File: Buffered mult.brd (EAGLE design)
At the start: 100.4 x 17.6 mm, 29 parts, among them IC1 OPA4171, IC3 OPA4171, J1 EURO_POWER_HEADERFAT_PADS

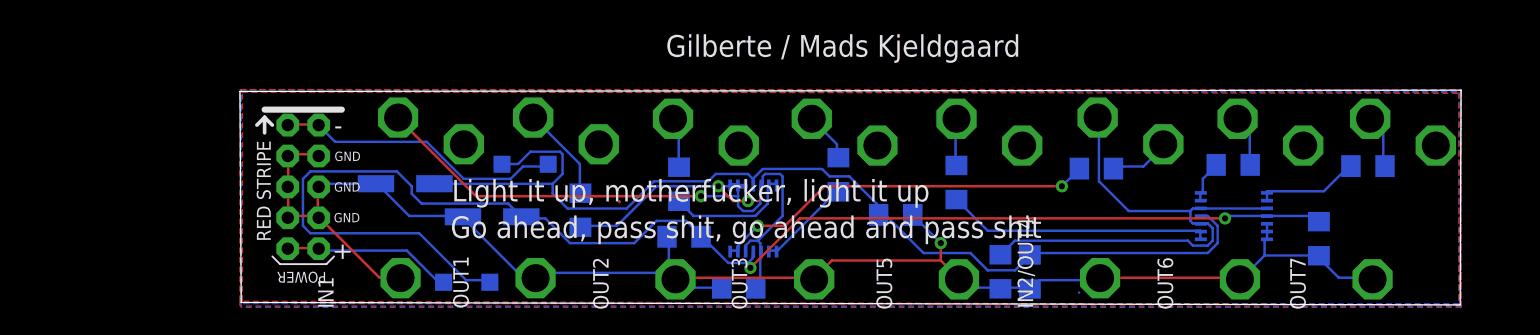
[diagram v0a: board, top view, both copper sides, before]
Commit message: new revision: Changed IC2 to opa2171, fixed switch jack
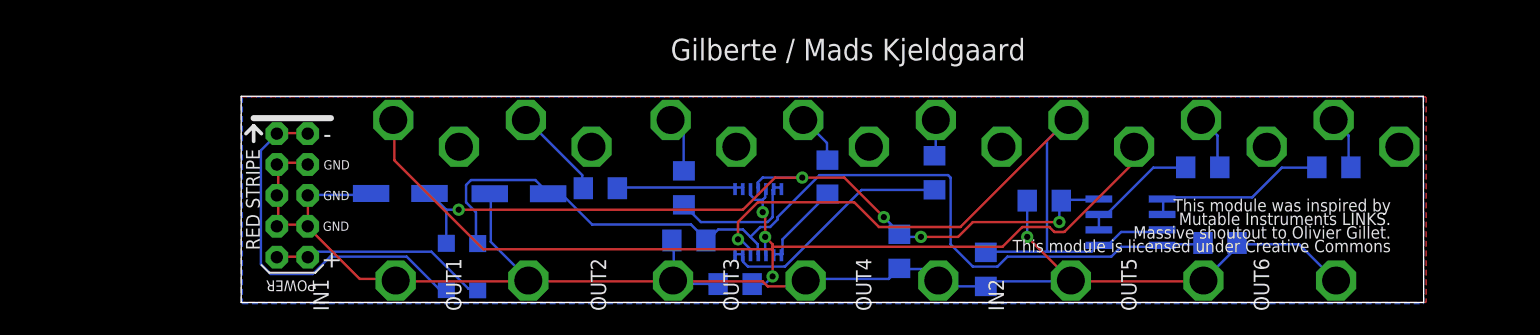
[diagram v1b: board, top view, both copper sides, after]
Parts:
- removed IC3: OPA4171, linear:TSSOP14
- removed IN2/OUT4, OUT7: PJ302M, pj302m:PJ302M
- removed R9: 51, SparkFun-Passives:1206
- added IC4: OPA2171, linear:SO08
- added IN2, OUT4: PJ302M, pj302m:PJ302M
- moved OUT5 20.1 mm to (79.1, -0.70)
- moved D1 10.6 mm to (16.9, 2.96), turned to 270 degrees
- moved C3 8.14 mm to (80.5, 4.89), turned to 0 degrees
- moved OUT6 7.90 mm to (90.0, -0.70)
- moved C2 5.98 mm to (66.0, 8.37), turned to 0 degrees
- moved C5 3.01 mm to (54.1, 4.20), turned to 270 degrees
- moved C13 2.91 mm to (22.8, 8.94)
- moved R6 2.80 mm to (89.8, 11.1)
- moved R5 2.51 mm to (79.0, 11.1)
- moved R3 2.44 mm to (29.5, 9.39), turned to 0 degrees
- moved R4 1.97 mm to (57.0, 10.7)
- moved D2 1.56 mm to (19.4, 2.94), turned to 90 degrees
- moved R8 1.22 mm to (61.2, 2.72)
- moved J1 1.14 mm to (4.20, 8.80)
- moved R2 0.92 mm to (48.2, 10.3)
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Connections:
- removed net N$16: IC1.13, IC1.14, R9.1
- removed net N$18: IN2/OUT4.SW, R9.2
- net GND: now also IN2.GND, OUT4.GND; no longer IC3.12, IC3.13, IC3.14, IN2/OUT4.GND, OUT7.GND
- net N$1: now also OUT6.TIP; no longer OUT7.TIP
- net N$12: now also IC4.1, IC4.2; no longer IC3.8, IC3.9
- net N$13: now also IC4.6, IC4.7; no longer IC3.6, IC3.7
- net N$17: now also IC1.13, IC1.14; no longer IC3.1, IC3.2
- net N$19: now also IC1.12, IC4.3, IC4.5, IN2.TIP; no longer IC3.10, IC3.3, IC3.5, IN2/OUT4.TIP
- net N$3: now also OUT5.TIP; no longer OUT6.TIP
- net N$4: now also OUT4.TIP; no longer OUT5.TIP
- net N$5: now also IN2.SW; no longer IC1.12
- net VCC: now also IC4.8; no longer IC3.4
- net VEE: now also IC4.4; no longer IC3.11
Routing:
- net VEE: track 113.4 -> 79.8 mm, vias 2 -> 0
- net N$5: track 51.4 -> 84.4 mm, vias 1 -> 3
- net N$16: track 31.9 -> 0.00 mm, vias 2 -> 0
- net N$19: track 42.4 -> 62.5 mm, vias 0 -> 1
- net VCC: track 84.2 -> 68.1 mm, vias 0 -> 5
- net N$2: track 18.7 -> 10.6 mm, vias 2 -> 0
- net N$15: track 23.9 -> 31.1 mm
- net N$13: track 3.56 -> 10.1 mm
- net N$12: track 8.59 -> 15.1 mm
- net N$18: track 5.11 -> 0.00 mm
- net N$14: track 14.0 -> 18.0 mm
- net N$17: track 21.8 -> 19.8 mm
- net GND: track 131.5 -> 133.0 mm
- net N$4: track 3.89 -> 3.01 mm
- net N$10: track 10.5 -> 11.2 mm
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- added copper zone on layer 1, net N$16
- removed copper zone on layer 1, net N$20
- removed copper zone on layer 16, net N$21
- removed copper zone on layer 1, net N$22
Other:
- board size 100.4 x 17.6 mm -> 97.2 x 16.9 mm
- board text added: "This module was inspired by Mutable Instruments LINKS. Massive shoutout to Olivier Gillet. This module is licensed under Creative Commons"
- board text removed: "Go ahead, pass shit, go ahead and pass shit"
- board text removed: "Light it up, motherfucker, light it up"

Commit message: small touchups
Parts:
- removed FRAME1: FRAME-LETTER, SparkFun-Aesthetics:CREATIVE_COMMONS
- moved IN1 1.04 mm to (13.7, -0.40)
- moved OUT1 1.04 mm to (24.6, -0.40)
- moved C13 0.30 mm to (22.8, 9.24)
- moved C2 0.30 mm to (66.0, 8.67)
- moved C3 0.30 mm to (80.5, 5.19)
- moved C7 0.30 mm to (36.8, 5.40)
- moved IC1 0.30 mm to (42.5, 6.90)
- moved IC4 0.30 mm to (73.1, 6.90)
- moved R1 0.30 mm to (36.4, 9.72)
- moved R4 0.30 mm to (57.0, 11.0)
- moved R5 0.30 mm to (79.0, 11.4)
- moved R6 0.30 mm to (89.8, 11.4)
- moved D2 0.30 mm to (19.4, 3.24)
- moved R7 0.30 mm to (40.6, 1.81)
- moved IN2 0.30 mm to (68.2, -0.40)
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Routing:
- net N$5: track 84.4 -> 81.2 mm
- net GND: track 133.0 -> 130.4 mm
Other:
- board size 97.2 x 16.9 mm -> 97.2 x 17.2 mm
- board text added: "This module was inspired by Mutable Instruments LINKS by Olivier Gillet and is licensed under cc-by-sa-3.0"
- board text removed: "Gilberte / Mads Kjeldgaard"
- board text removed: "This module was inspired by Mutable Instruments LINKS. Massive shoutout to Olivier Gillet. This module is licensed under Creative Commons"
